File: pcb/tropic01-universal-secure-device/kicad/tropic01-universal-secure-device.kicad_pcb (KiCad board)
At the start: 4 copper layers, 52 x 82 mm, 55 parts, among them J1 USB4105-GF-A, J2 54132-4062, J2B 52271-0679, J3 FTSH-103-01-F-DV-K, J5 FTSH-105-01-F-DV-K, J6 SM04B-SRSS-TB, J7 FTSH-104-01-F-DV-K, J8 FTSH-106-01-F-DV-K, J9 S2B-PH-SM4-TB, SW1 EVQP7J01P, SW2 EVQP7J01P, U1 STM32U585VIT6, U10 BQ24074RGTR, U11 OPTIGA-TRUST-M-SLS32AIA, U13 TPS22917DBVR, U15 TPS61165DBVR, U2 TR01-C2P-T301, U3 TPS62840DLCR, U4 TPS22917DBVR, U5 W25Q128JVSIQ, U6 TMUX1574RSVR, U7 TPD4E05U06DQAR, U8 TPS2553DBVR, U9 ST25R3916B-AQET, X1 16MHz, X3 FA-238 27.12MHz

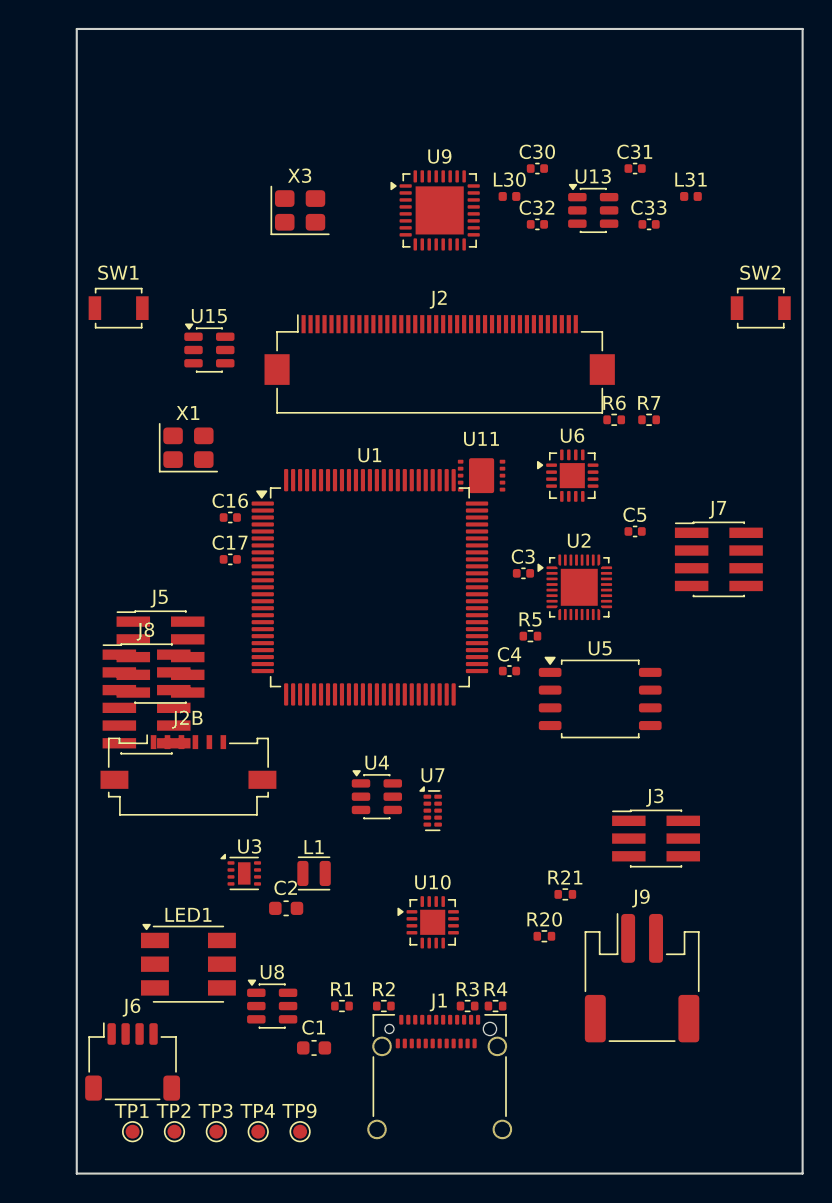
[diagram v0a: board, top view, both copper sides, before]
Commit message: feat: apply compact tropic01 board placement
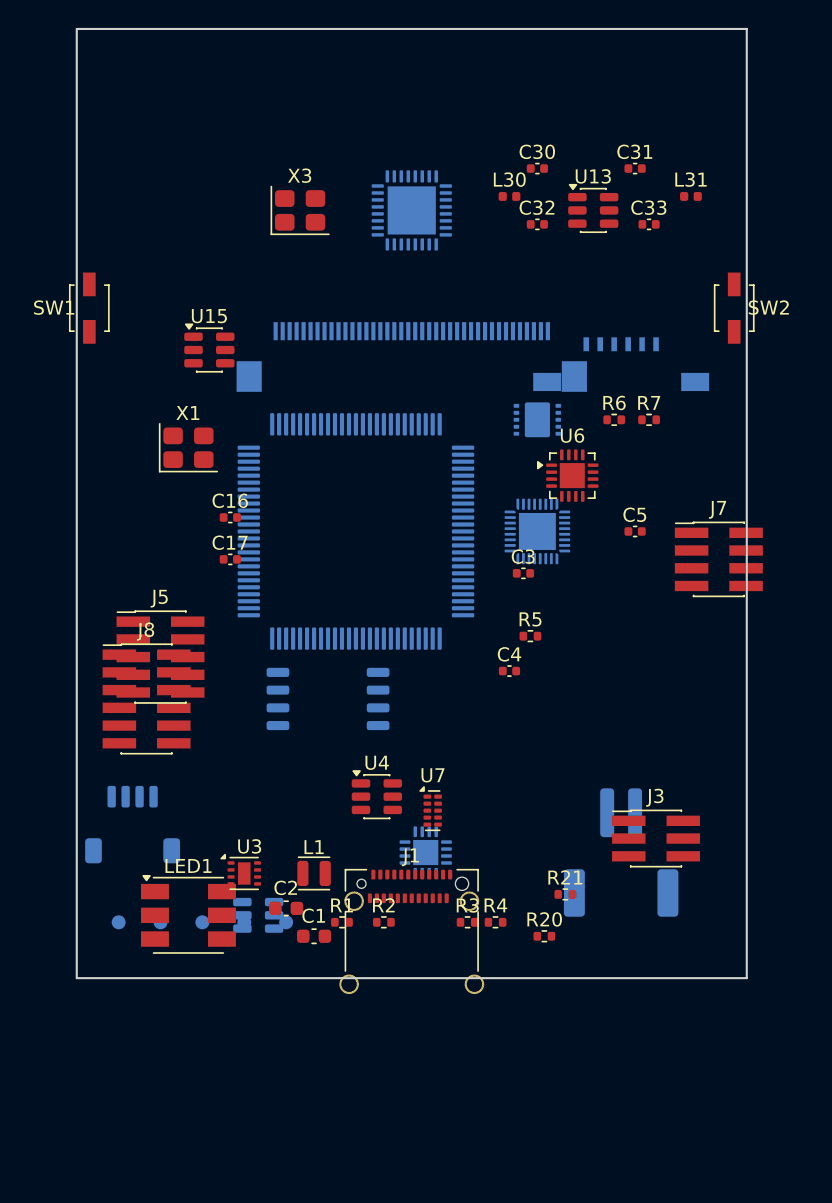
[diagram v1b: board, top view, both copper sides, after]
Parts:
- J2, J2B, J6, J9, TP1, TP2, TP3, TP4, TP9, U1, U11, U2, U8, U9: moved to B.Cu
- U10: footprint Package_DFN_QFN:VQFN-16-1EP_3x3mm_P0.5mm_EP1.8x1.8mm -> Package_DFN_QFN:VQFN-16-1EP_3.5x3.5mm_P0.5mm_EP2.1x2.1mm; moved to B.Cu
- U5: footprint Package_SO:SOIC-8_5.3x5.3mm_P1.27mm -> Package_SO:SOIC-8_5.23x5.23mm_P1.27mm; moved to B.Cu
- moved J2B 42.1 mm to (49.0, 33.5)
- moved U5 19.5 mm to (28.0, 58.0)
- moved J6 17.0 mm to (14.0, 67.0)
- moved TP1 15.0 mm to (13.0, 74.0)
- moved TP2 15.0 mm to (16.0, 74.0)
- moved TP3 15.0 mm to (19.0, 74.0)
- moved TP4 15.0 mm to (22.0, 74.0)
- moved TP9 15.0 mm to (25.0, 74.0)
- moved J1 10.6 mm to (34.0, 75.6)
- moved J9 9.12 mm to (49.0, 69.0)
- moved C1 8.00 mm to (27.0, 75.0)
- moved U8 6.58 mm to (23.0, 73.5)
- moved R1 6.00 mm to (29.0, 74.0)
- moved R2 6.00 mm to (32.0, 74.0)
- moved R3 6.00 mm to (38.0, 74.0)
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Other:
- board size 52 x 82 mm -> 48 x 68 mm

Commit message: feat: bind tropic01 pcb nets
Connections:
- J1 pad A1: (no net) -> GND
- J1 pad A12: (no net) -> GND
- J1 pad A4: (no net) -> VBUS
- J1 pad A5: (no net) -> USB_CC1_RD
- J1 pad A6: (no net) -> USB_DP
- J1 pad A7: (no net) -> USB_DM
- J1 pad A9: (no net) -> VBUS
- J1 pad B1: (no net) -> GND
- J1 pad B12: (no net) -> GND
- J1 pad B4: (no net) -> VBUS
- J1 pad B5: (no net) -> USB_CC2_RD
- J1 pad B6: (no net) -> USB_DP
- J1 pad B7: (no net) -> USB_DM
- J1 pad B9: (no net) -> VBUS
- J2 pad 1: (no net) -> GND
- J2 pad 10: (no net) -> TFT_CS
- J2 pad 11: (no net) -> TFT_DC
- J2 pad 12: (no net) -> TFT_SPI_SCK
- J2 pad 30: (no net) -> TFT_RST
- J2 pad 31: (no net) -> GND
- J2 pad 32: (no net) -> DISPLAY_VCC_SW
- J2 pad 33: (no net) -> DISPLAY_VCC_SW
- J2 pad 34: (no net) -> TFT_BACKLIGHT_K
- J2 pad 35: (no net) -> TFT_BACKLIGHT_K
- J2 pad 36: (no net) -> TFT_BACKLIGHT_K
- J2 pad 37: (no net) -> TFT_BACKLIGHT_K
- J2 pad 38: (no net) -> TFT_BACKLIGHT_A
- J2 pad 39: (no net) -> GND
- J2 pad 7: (no net) -> DISPLAY_VCC_SW
- J2 pad 8: (no net) -> DISPLAY_VCC_SW
- J2 pad 9: (no net) -> TFT_SPI_MOSI
- J2B pad 1: (no net) -> DISPLAY_VCC_SW
- J2B pad 2: (no net) -> GND
- J2B pad 3: (no net) -> TOUCH_I2C_SCL
- J2B pad 4: (no net) -> TOUCH_I2C_SDA
- J2B pad 5: (no net) -> TOUCH_INT
- J2B pad 6: (no net) -> TOUCH_RST
- J9 pad 1: (no net) -> VBAT
- J9 pad 2: (no net) -> GND
- SW1 pad 1: (no net) -> BTN_LEFT
- SW1 pad 2: (no net) -> GND
- SW2 pad 1: (no net) -> BTN_RIGHT
- SW2 pad 2: (no net) -> GND
- U1 pad 1: (no net) -> BTN_LEFT
- U1 pad 14: (no net) -> NRST
- U1 pad 2: (no net) -> BTN_RIGHT
- U1 pad 29: (no net) -> TROPIC_SPI_CSN
- U1 pad 30: (no net) -> TROPIC_SPI_SCK
- U1 pad 31: (no net) -> TROPIC_SPI_MISO
- U1 pad 32: (no net) -> TROPIC_SPI_MOSI
- U1 pad 35: (no net) -> TROPIC_PWR_EN
- U1 pad 36: (no net) -> NFC_PWR_EN
- U1 pad 37: (no net) -> TROPIC_GPO
- U1 pad 41: (no net) -> QSPI_CLK
- U1 pad 42: (no net) -> QSPI_NCS
- U1 pad 43: (no net) -> QSPI_IO0
- U1 pad 44: (no net) -> QSPI_IO1
- U1 pad 45: (no net) -> QSPI_IO2
- U1 pad 46: (no net) -> QSPI_IO3
- U1 pad 51: (no net) -> NFC_SPI_CSN
- U1 pad 52: (no net) -> NFC_SPI_SCK
- U1 pad 53: (no net) -> NFC_SPI_MISO
- U1 pad 54: (no net) -> NFC_SPI_MOSI
- U1 pad 63: (no net) -> TFT_RST
- U1 pad 64: (no net) -> TFT_CS
- U1 pad 65: (no net) -> TFT_DC
- U1 pad 66: (no net) -> TFT_PWR_EN
- U1 pad 67: (no net) -> TFT_BACKLIGHT_PWM
- U1 pad 68: (no net) -> USB_VBUS_SENSE
- U1 pad 70: (no net) -> USB_DM
- U1 pad 71: (no net) -> USB_DP
- U1 pad 72: (no net) -> SWDIO
- U1 pad 76: (no net) -> SWCLK
- U1 pad 78: (no net) -> TFT_SPI_SCK
- U1 pad 80: (no net) -> TFT_SPI_MOSI
- U1 pad 81: (no net) -> NFC_IRQ
- U1 pad 86: (no net) -> EXP_UART_TX
- U1 pad 87: (no net) -> EXP_UART_RX
- U1 pad 91: (no net) -> SE2_RST
- U1 pad 92: (no net) -> SE2_I2C_SCL
- U1 pad 93: (no net) -> SE2_I2C_SDA
- U1 pad 94: (no net) -> BOOT0
- U1 pad 95: (no net) -> TOUCH_I2C_SCL
- U1 pad 96: (no net) -> TOUCH_I2C_SDA
- U1 pad 97: (no net) -> TOUCH_RST
- U1 pad 98: (no net) -> TOUCH_INT
- U11 pad 1: (no net) -> GND
- U11 pad 10: (no net) -> SYS_3V3
- U11 pad 3: (no net) -> SE2_I2C_SDA
- U11 pad 8: (no net) -> SE2_I2C_SCL
- U11 pad 9: (no net) -> SE2_RST
- U2 pad 1: (no net) -> TROPIC_VCC_SW
- U2 pad 11: (no net) -> TROPIC_VCC_SW
- U2 pad 12: (no net) -> GND
- U2 pad 2: (no net) -> GND
- U2 pad 23: (no net) -> GND
- U2 pad 24: (no net) -> TROPIC_VCC_SW
- U2 pad 4: (no net) -> TROPIC_GPO
- U2 pad 5: (no net) -> TROPIC_SPI_MOSI
- U2 pad 6: (no net) -> TROPIC_SPI_MISO
- U2 pad 7: (no net) -> TROPIC_SPI_SCK
- U2 pad 8: (no net) -> TROPIC_SPI_CSN
- U5 pad 1: (no net) -> QSPI_NCS
- U5 pad 2: (no net) -> QSPI_IO1
- U5 pad 3: (no net) -> QSPI_IO2
- U5 pad 4: (no net) -> GND
- U5 pad 5: (no net) -> QSPI_IO0
- U5 pad 6: (no net) -> QSPI_CLK
- U5 pad 7: (no net) -> QSPI_IO3
- U5 pad 8: (no net) -> SYS_3V3
- U9 pad 1: (no net) -> NFC_VCC_SW
- U9 pad 10: (no net) -> NFC_VCC_SW
- U9 pad 12: (no net) -> GND
- U9 pad 16: (no net) -> GND
- U9 pad 20: (no net) -> GND
- U9 pad 21: (no net) -> GND
- U9 pad 26: (no net) -> GND
- U9 pad 27: (no net) -> NFC_IRQ
- U9 pad 29: (no net) -> NFC_SPI_CSN
- U9 pad 30: (no net) -> NFC_SPI_SCK
- U9 pad 31: (no net) -> NFC_SPI_MOSI
- U9 pad 32: (no net) -> NFC_SPI_MISO
- U9 pad 33: (no net) -> GND
- U9 pad 6: (no net) -> GND
- U9 pad 8: (no net) -> NFC_VCC_SW

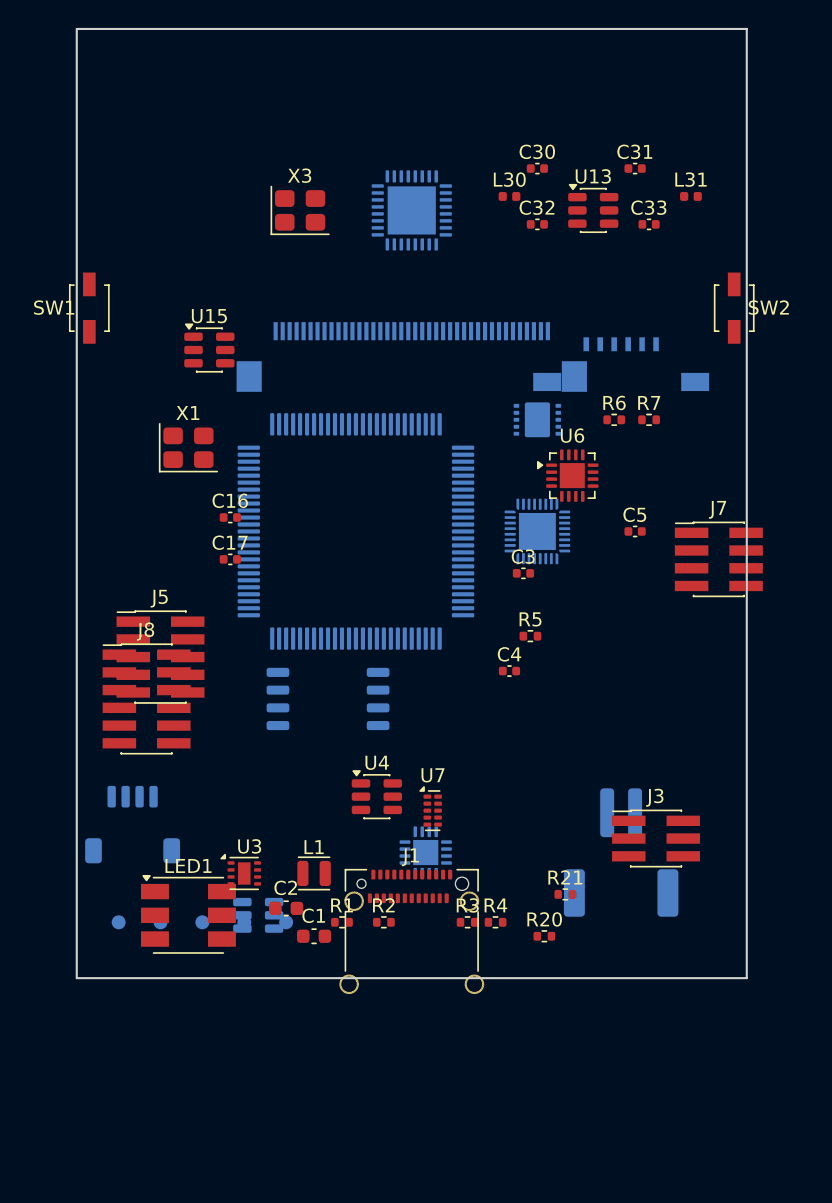
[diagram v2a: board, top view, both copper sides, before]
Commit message: hardware: preserve PCB GUI WIP and tropic01 helper scripts
Capture the in-progress .kicad_pcb footprint rework (side-actuated
EVQP7C switches, real JST/connector footprints, removal of stale
expansion headers J3/J5/J7/J8) and four helper scripts
(check_tropic01_clean_baseline, check_tropic01_placement_overlaps,
update_tropic01_universal_erc_triage, update_tropic01_universal_preflight_summary)
so all work is committed before consolidating onto main.
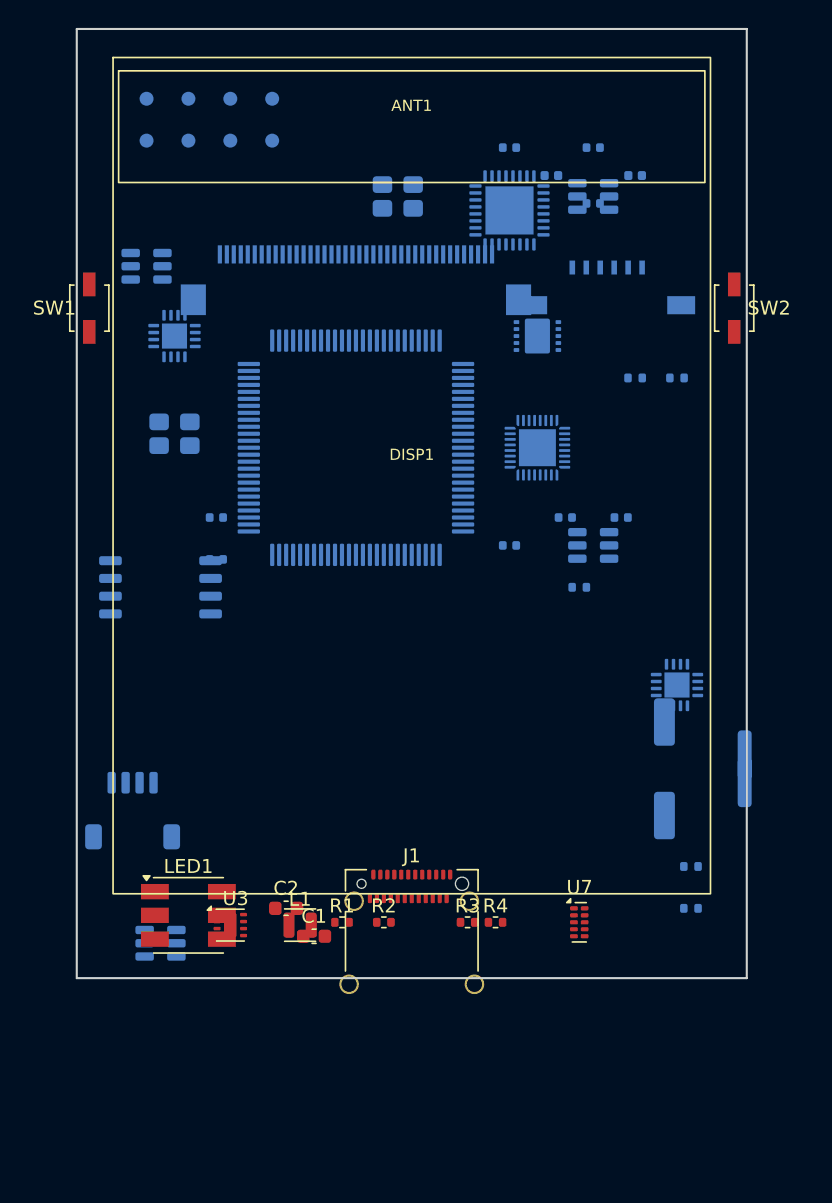
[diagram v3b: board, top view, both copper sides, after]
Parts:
- removed J3: FTSH-103-01-F-DV-K, Connector_PinHeader_1.27mm:PinHeader_2x03_P1.27mm_Vertical_SMD
- removed J5: FTSH-105-01-F-DV-K, Connector_PinHeader_1.27mm:PinHeader_2x05_P1.27mm_Vertical_SMD
- removed J7: FTSH-104-01-F-DV-K, Connector_PinHeader_1.27mm:PinHeader_2x04_P1.27mm_Vertical_SMD
- removed J8: FTSH-106-01-F-DV-K, Connector_PinHeader_1.27mm:PinHeader_2x06_P1.27mm_Vertical_SMD
- removed TP1: VBUS, TestPoint:TestPoint_Pad_D1.0mm
- removed TP2: 3V3, TestPoint:TestPoint_Pad_D1.0mm
- removed TP3: GND, TestPoint:TestPoint_Pad_D1.0mm
- removed TP4: USB_DP, TestPoint:TestPoint_Pad_D1.0mm
- removed TP9: USB_DM, TestPoint:TestPoint_Pad_D1.0mm
- added ANT1: 13.56MHz_NFC_ANTENNA_ENVELOPE, nSealr_Mechanical:NFC_Antenna_Envelope_42x8mm, F.Cu at (34.0, 17.0)
- added BAT1: LiPo_301020_REAR_ENVELOPE, nSealr_Mechanical:LiPo_301020_Rear_Envelope_30x20mm, B.Cu at (33.0, 63.0)
- added DISP1: NHD-2.4-240320AF-CSXP-CTP, Mechanical:Display_Envelope_42.8x59.91mm, F.Cu at (34.0, 42.0)
- added TP_3V3: 3V3, TestPoint:TestPoint_Pad_D1.0mm, B.Cu at (21.0, 18.0)
- added TP_BOOT0: BOOT0, TestPoint:TestPoint_Pad_D1.0mm, B.Cu at (24.0, 15.0)
- added TP_GND: GND, TestPoint:TestPoint_Pad_D1.0mm, B.Cu at (24.0, 18.0)
- added TP_NRST: NRST, TestPoint:TestPoint_Pad_D1.0mm, B.Cu at (21.0, 15.0)
- added TP_SWCLK: SWCLK, TestPoint:TestPoint_Pad_D1.0mm, B.Cu at (18.0, 15.0)
- added TP_SWDIO: SWDIO, TestPoint:TestPoint_Pad_D1.0mm, B.Cu at (15.0, 15.0)
- added TP_UART_RX: UART_RX, TestPoint:TestPoint_Pad_D1.0mm, B.Cu at (18.0, 18.0)
- added TP_UART_TX: UART_TX, TestPoint:TestPoint_Pad_D1.0mm, B.Cu at (15.0, 18.0)
- C16, C17, C3, C30, C31, C32, C33, C4, C5, L30, L31, R20, R21, R5, R6, R7, U13, U15, U4, U6, X1, X3: moved to B.Cu
- SW1, SW2: footprint Button_Switch_SMD:SW_SPST_EVQP7A -> Button_Switch_SMD:SW_SPST_EVQP7C
- moved U6 30.2 mm to (17.0, 32.0)
- moved U4 23.8 mm to (47.0, 47.0)
- moved U10 21.6 mm to (53.0, 57.0)
- moved U5 14.4 mm to (16.0, 50.0)
- moved U7 13.2 mm to (46.0, 74.0)
- moved C4 11.7 mm to (45.0, 45.0)
- moved R20 11.6 mm to (54.0, 70.0)
- moved R21 9.06 mm to (54.0, 73.0)
- moved J9 8.49 mm to (55.0, 63.0), turned to 270 degrees
- moved U15 7.50 mm to (15.0, 27.0)
- moved U8 7.28 mm to (16.0, 75.5)
- moved X3 7.07 mm to (33.0, 22.0)
- moved U9 7.00 mm to (41.0, 23.0)
- moved J2 6.80 mm to (30.0, 28.0)
- moved U1 6.00 mm to (30.0, 40.0)
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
